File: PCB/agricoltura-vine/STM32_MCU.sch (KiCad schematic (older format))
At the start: 33 parts, among them SW1 B3U-1000P, T1 BU2032SM-JJ-GTR, T2 20021121-00010C4LF, T3 0675031020, U1 STM32F446RET6, X1 ABM3B-8.000MHZ-B2-T, X2 ABS07-32.768KHZ-9-T

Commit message: Route Started Connectors Changed
Changed to QWIIC style connectors and adjusted pinning of RJ45s, but switching to screw terminal header in next commit. THis is a backup
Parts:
- removed SW1: B3U-1000P, AVR-KiCAD-Lib-Mech-Switches:B3U-1000P, symbol AVR-KiCAD-Lib-Mech-Switches:B3U-1000P
- added SW1: TL3301NF260QG, AVR-KiCAD-Lib-Mech-Switches:TL3301NF260QG, symbol AVR-KiCAD-Lib-Mech-Switches:TL3301NF260QG
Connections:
- net labels added: D+, D-, ID, NRST, OSC32_IN, OSC32_OUT, OSC_IN, OSC_OUT, VBUS, VCAP1
- wire segments 117 -> 124
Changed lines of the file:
@@
-	1    0    0    -1
-$EndComp
-$Comp
-L AVR-KiCAD-Lib-Mech-Switches:B3U-1000P SW1
-U 1 1 5EEC10BD
-P 5600 5400
-F 0 "SW1" H 5600 5550 50  0000 C CNN
-F 1 "B3U-1000P" H 5650 5350 50  0000 C CNN
-F 2 "AVR-KiCAD-Lib-Mech-Switches:B3U-1000P" H 5600 5400 50  0001 C CNN
-F 3 "https://omronfs.omron.com/en_US/ecb/products/pdf/en-b3u.pdf" H 5600 5400 50  0001 C CNN
-F 4 "0.98000" H 5700 5650 50  0001 C CNN "Cost QTY: 1"
-F 5 "0.59822" H 5800 5750 50  0001 C CNN "Cost QTY: 1000"
-F 6 "*" H 5900 5850 50  0001 C CNN "Cost QTY: 2500"
-F 7 "*" H 6000 5950 50  0001 C CNN "Cost QTY: 5000"
-F 8 "*" H 6100 6050 50  0001 C CNN "Cost QTY: 10000"
-F 9 "Omron Electronics Inc-EMC Div" H 6200 6150 50  0001 C CNN "MFR"
-F 10 "B3U-1000P" H 6300 6250 50  0001 C CNN "MFR#"
-F 11 "Digikey" H 6400 6350 50  0001 C CNN "Vendor"
-F 12 "SW1020CT-ND" H 6500 6450 50  0001 C CNN "Vendor #"
-F 13 "AVR" H 6600 6550 50  0001 C CNN "Designer"
-F 14 "1.6mm" H 6700 6650 50  0001 C CNN "Height"
-F 15 "6/15/2020" H 7800 7750 50  0001 C CNN "Date Created"
-F 16 "6/15/2020" H 6800 6750 50  0001 C CNN "Date Modified"
-F 17 "Yes" H 6900 6850 50  0001 C CNN "Lead-Free ?"
-F 18 "1" H 7000 6950 50  0001 C CNN "RoHS Levels"
-F 19 "SMT" H 7100 7050 50  0001 C CNN "Mounting"
-F 20 "2" H 7200 7150 50  0001 C CNN "Pin Count #"
-F 21 "Active" H 7300 7250 50  0001 C CNN "Status"
-F 22 "*" H 7400 7350 50  0001 C CNN "Tolerance"
-F 23 "Switch" H 7500 7450 50  0001 C CNN "Type"
-F 24 "*" H 7600 7550 50  0001 C CNN "Voltage"
-F 25 "Proprietary" H 7700 7700 50  0001 C CNN "Package"
-F 26 "Tactile Switch SPST-NO Top Actuated Surface Mount" H 8000 8000 50  0001 C CNN "Description"
-F 27 "B3U-1000P" H 7900 7900 50  0001 C CNN "_Value_"
-F 28 "*" H 8000 8000 50  0001 C CNN "Management_ID"
-	1    5600 5400
 	1    0    0    -1
 $EndComp
@@
 L power:GND #PWR010
 U 1 1 5EF64659
-P 5900 5850
-F 0 "#PWR010" H 5900 5600 50  0001 C CNN
-F 1 "GND" H 5905 5677 50  0000 C CNN
-F 2 "" H 5900 5850 50  0001 C CNN
-F 3 "" H 5900 5850 50  0001 C CNN
-	1    5900 5850
-	1    0    0    -1
-$EndComp
-Wire Wire Line
-	5900 5400 5900 5850
-Wire Wire Line
-	5900 5850 5300 5850
-Connection ~ 5900 5850
+P 6250 5950
+F 0 "#PWR010" H 6250 5700 50  0001 C CNN
+F 1 "GND" H 6255 5777 50  0000 C CNN
+F 2 "" H 6250 5950 50  0001 C CNN
+F 3 "" H 6250 5950 50  0001 C CNN
+	1    6250 5950
+	1    0    0    -1
+$EndComp
+Wire Wire Line
+	6250 5500 6250 5950
+Wire Wire Line
+	6250 5950 5650 5950
+Connection ~ 6250 5950
 $Comp
 L AVR-KiCAD-Lib-Capacitors:C0402C104K9PACTU C13
@@
 	1    0    0    -1
 $EndComp
+Text Label 8800 2950 0    50   ~ 0
+D-
+Text Label 8800 3050 0    50   ~ 0
+D+
+Text Label 8800 3150 0    50   ~ 0
+ID
+Text Label 8800 2850 0    50   ~ 0
+VBUS
+Text Label 4650 5400 0    50   ~ 0
+NRST
+Text Label 1650 5400 0    50   ~ 0
+OSC_IN
+Text Label 1650 5550 0    50   ~ 0
+OSC_OUT
+Text Label 6850 3850 0    50   ~ 0
+OSC32_IN
+Text Label 6650 4500 1    50   ~ 0
+OSC32_OUT
+Text Label 7550 4100 1    50   ~ 0
+VCAP1
+$Comp
+L AVR-KiCAD-Lib-Mech-Switches:TL3301NF260QG SW1
+U 1 1 5EF8B26F
+P 5950 5400
+F 0 "SW1" H 5950 5550 50  0000 C CNN
+F 1 "TL3301NF260QG" H 6600 5250 50  0000 C CNN
+F 2 "AVR-KiCAD-Lib-Mech-Switches:TL3301NF260QG" H 5950 5400 50  0001 C CNN
+F 3 "http://spec_sheets.e-switch.com/specs/P010517.pdf" H 5950 5400 50  0001 C CNN
+F 4 "0.38000" H 6050 5650 50  0001 C CNN "Cost QTY: 1"
+F 5 "*" H 6150 5750 50  0001 C CNN "Cost QTY: 1000"
+F 6 "*" H 6250 5850 50  0001 C CNN "Cost QTY: 2500"
+F 7 "*" H 6350 5950 50  0001 C CNN "Cost QTY: 5000"
+F 8 "*" H 6450 6050 50  0001 C CNN "Cost QTY: 10000"
+F 9 "E-Switch" H 6550 6150 50  0001 C CNN "MFR"
+F 10 "TL3301NF260QG" H 6650 6250 50  0001 C CNN "MFR#"
+F 11 "Digikey" H 6750 6350 50  0001 C CNN "Vendor"
+F 12 "EG1868TR-ND" H 6850 6450 50  0001 C CNN "Vendor #"
+F 13 "AVR" H 6950 6550 50  0001 C CNN "Designer"
+F 14 "4.4mm" H 7050 6650 50  0001 C CNN "Height"
+F 15 "2/28/2020" H 8150 7750 50  0001 C CNN "Date Created"
+F 16 "2/28/2020" H 7150 6750 50  0001 C CNN "Date Modified"
+F 17 "Yes" H 7250 6850 50  0001 C CNN "Lead-Free ?"
+F 18 "1" H 7350 6950 50  0001 C CNN "RoHS Levels"
+F 19 "SMT" H 7450 7050 50  0001 C CNN "Mounting"
+F 20 "4" H 7550 7150 50  0001 C CNN "Pin Count #"
+F 21 "Active" H 7650 7250 50  0001 C CNN "Status"
+F 22 "*" H 7750 7350 50  0001 C CNN "Tolerance"
+F 23 "Mechanical Momentary Switch " H 7850 7450 50  0001 C CNN "Type"
+F 24 "12VDC" H 7950 7550 50  0001 C CNN "Voltage"
+F 25 "Proprietary" H 8050 7700 50  0001 C CNN "Package"
+F 26 "Tactile Switch SPST-NO Top Actuated Surface Mount" H 8350 8000 50  0001 C CNN "Description"
+F 27 "TL3301NF260QG" H 8250 7900 50  0001 C CNN "_Value_"
+F 28 "*" H 8350 8000 50  0001 C CNN "Management_ID"
+	1    5950 5400
+	1    0    0    -1
+$EndComp
+Wire Wire Line
+	5650 5950 5650 5500
+Wire Wire Line
+	5300 5400 5650 5400
+Wire Wire Line
+	5650 5400 5650 5150
+Wire Wire Line
+	5650 5150 6250 5150
+Wire Wire Line
+	6250 5150 6250 5400
+Connection ~ 5650 5400
+Wire Wire Line
+	5300 5850 5300 5950
+Wire Wire Line
+	5300 5950 5650 5950
+Connection ~ 5650 5950
 $EndSCHEMATC

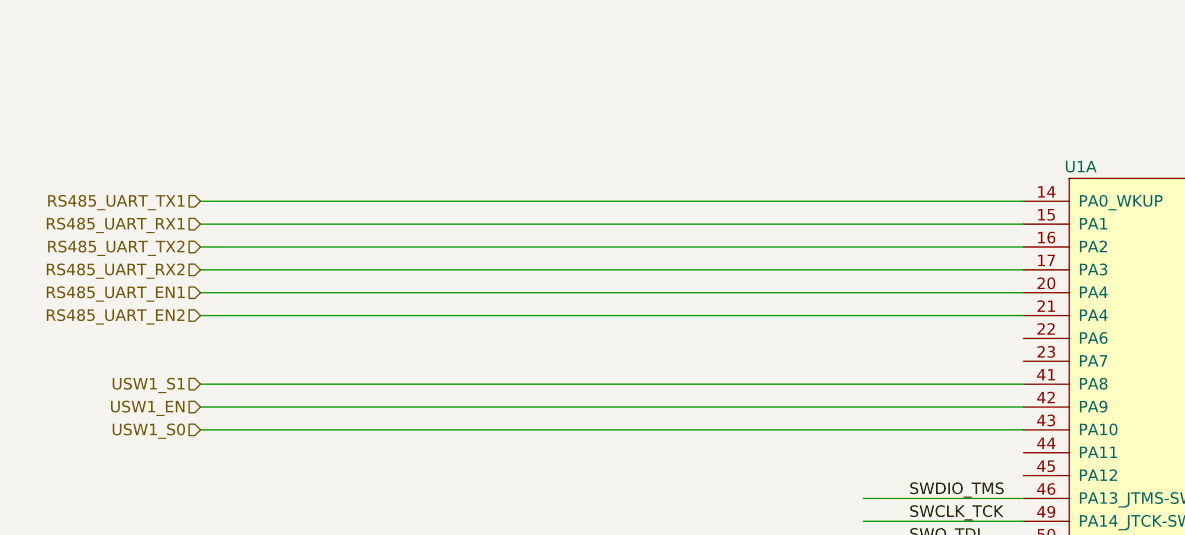
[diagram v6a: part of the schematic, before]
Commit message: Routing and New RS485
swapped over the RS485 chip to a new one and started routing the board.
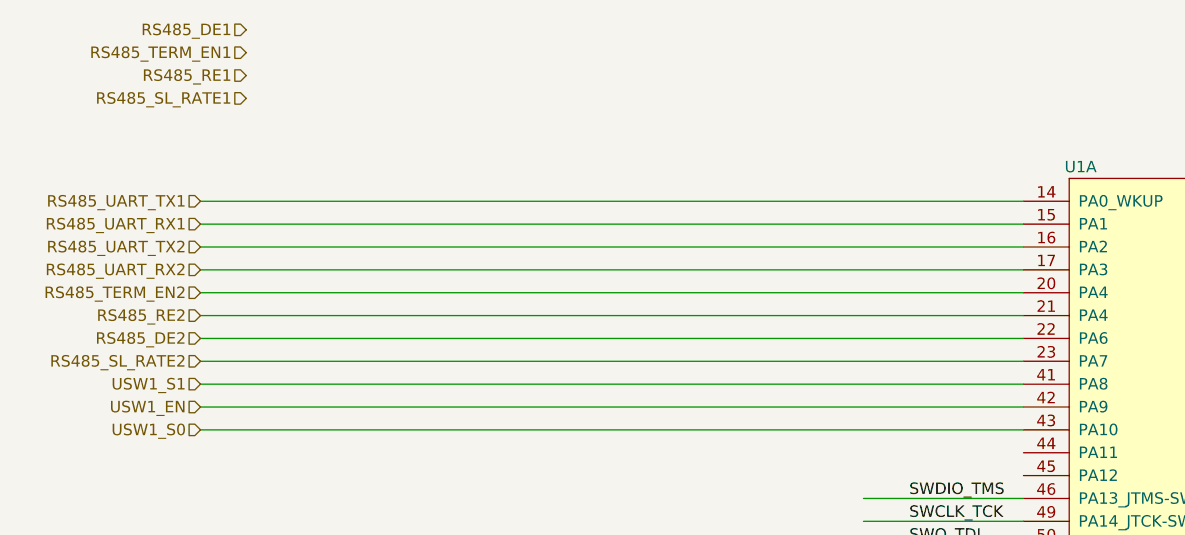
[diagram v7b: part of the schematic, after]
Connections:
- net labels added: RS485_DE1, RS485_DE2, RS485_RE1, RS485_RE2, RS485_SL_RATE1, RS485_SL_RATE2, RS485_TERM_EN1, RS485_TERM_EN2
- net labels removed: RS485_UART_EN1, RS485_UART_EN2
- wire segments 124 -> 126
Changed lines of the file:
@@
 Text HLabel 1200 3850 0    50   Input ~ 0
 UART_SENSE1_TX
-Text HLabel 1200 1950 0    50   Input ~ 0
-RS485_UART_EN1
 Text HLabel 1200 1550 0    50   Input ~ 0
 RS485_UART_TX1
 Text HLabel 1200 1650 0    50   Input ~ 0
 RS485_UART_RX1
-Text HLabel 1200 2050 0    50   Input ~ 0
-RS485_UART_EN2
 Text HLabel 1200 1750 0    50   Input ~ 0
 RS485_UART_TX2
@@
 	4800 1850 1200 1850
 Wire Wire Line
-	1200 1950 4800 1950
-Wire Wire Line
-	4800 2050 1200 2050
-Wire Wire Line
 	4800 3950 1200 3950
 Wire Wire Line
@@
 	5300 5950 5650 5950
 Connection ~ 5650 5950
+Text HLabel 1400 800  0    50   Input ~ 0
+RS485_DE1
+Text HLabel 1200 2150 0    50   Input ~ 0
+RS485_DE2
+Text HLabel 1400 900  0    50   Input ~ 0
+RS485_TERM_EN1
+Text HLabel 1400 1100 0    50   Input ~ 0
+RS485_SL_RATE1
+Text HLabel 1400 1000 0    50   Input ~ 0
+RS485_RE1
+Text HLabel 1200 2250 0    50   Input ~ 0
+RS485_SL_RATE2
+Text HLabel 1200 2050 0    50   Input ~ 0
+RS485_RE2
+Text HLabel 1200 1950 0    50   Input ~ 0
+RS485_TERM_EN2
+Wire Wire Line
+	4800 1950 1200 1950
+Wire Wire Line
+	1200 2050 4800 2050
+Wire Wire Line
+	1200 2150 4800 2150
+Wire Wire Line
+	4800 2250 1200 2250
 $EndSCHEMATC

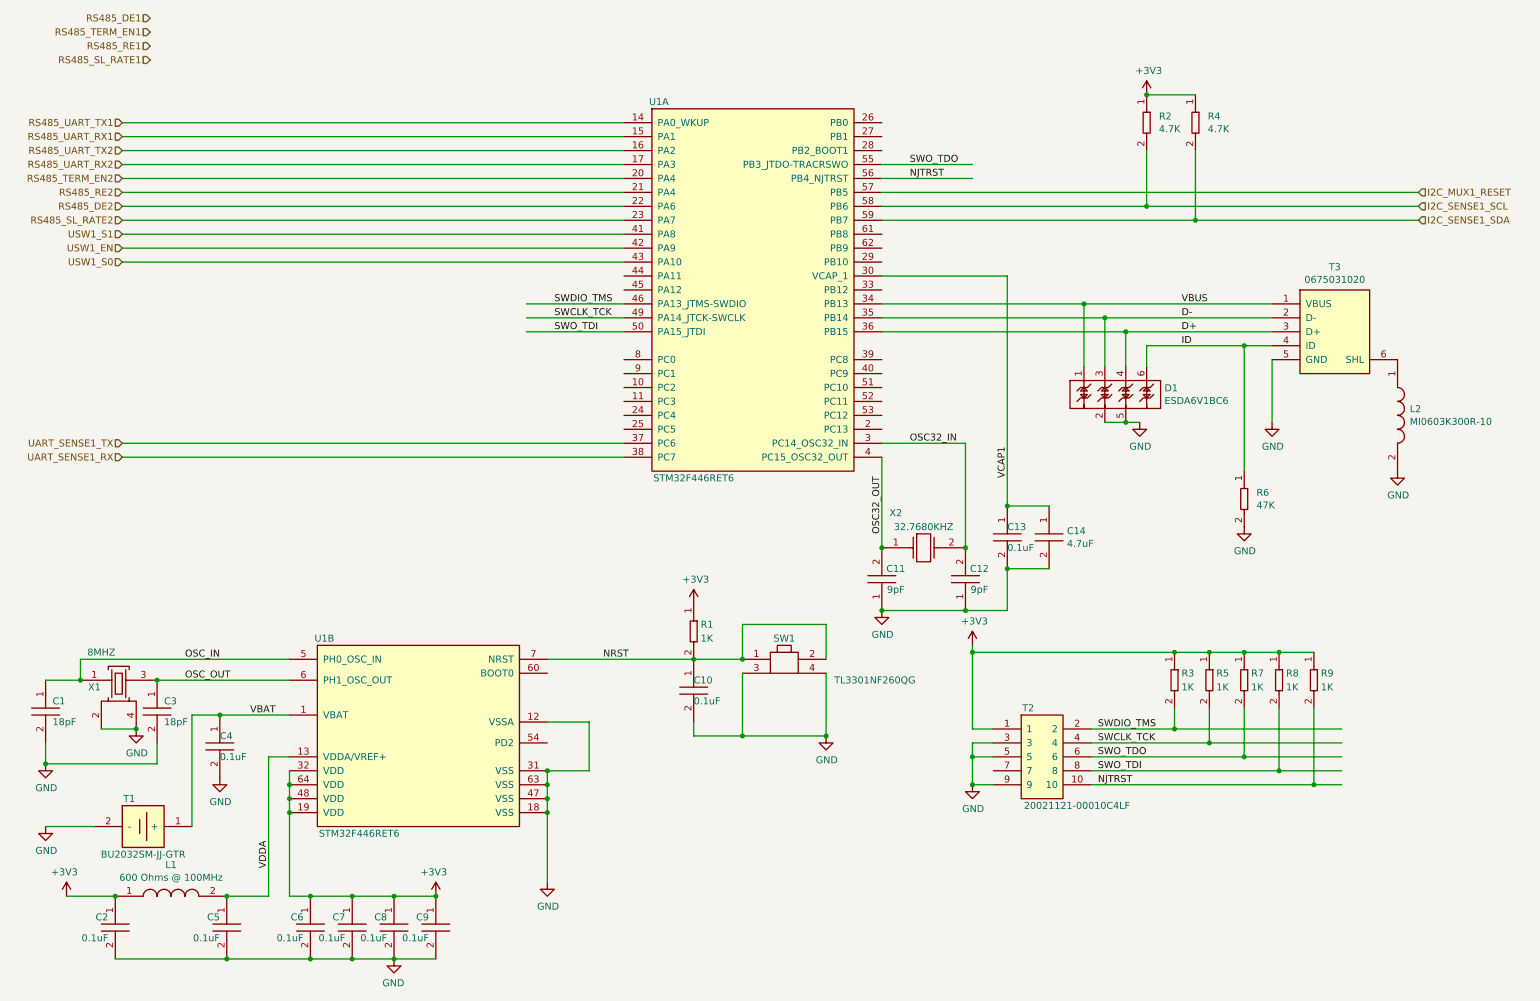
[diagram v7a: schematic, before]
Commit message: Routing progress
RS845 ports routed, UART mux routed, sensor ports reoriented. Starting to come together.
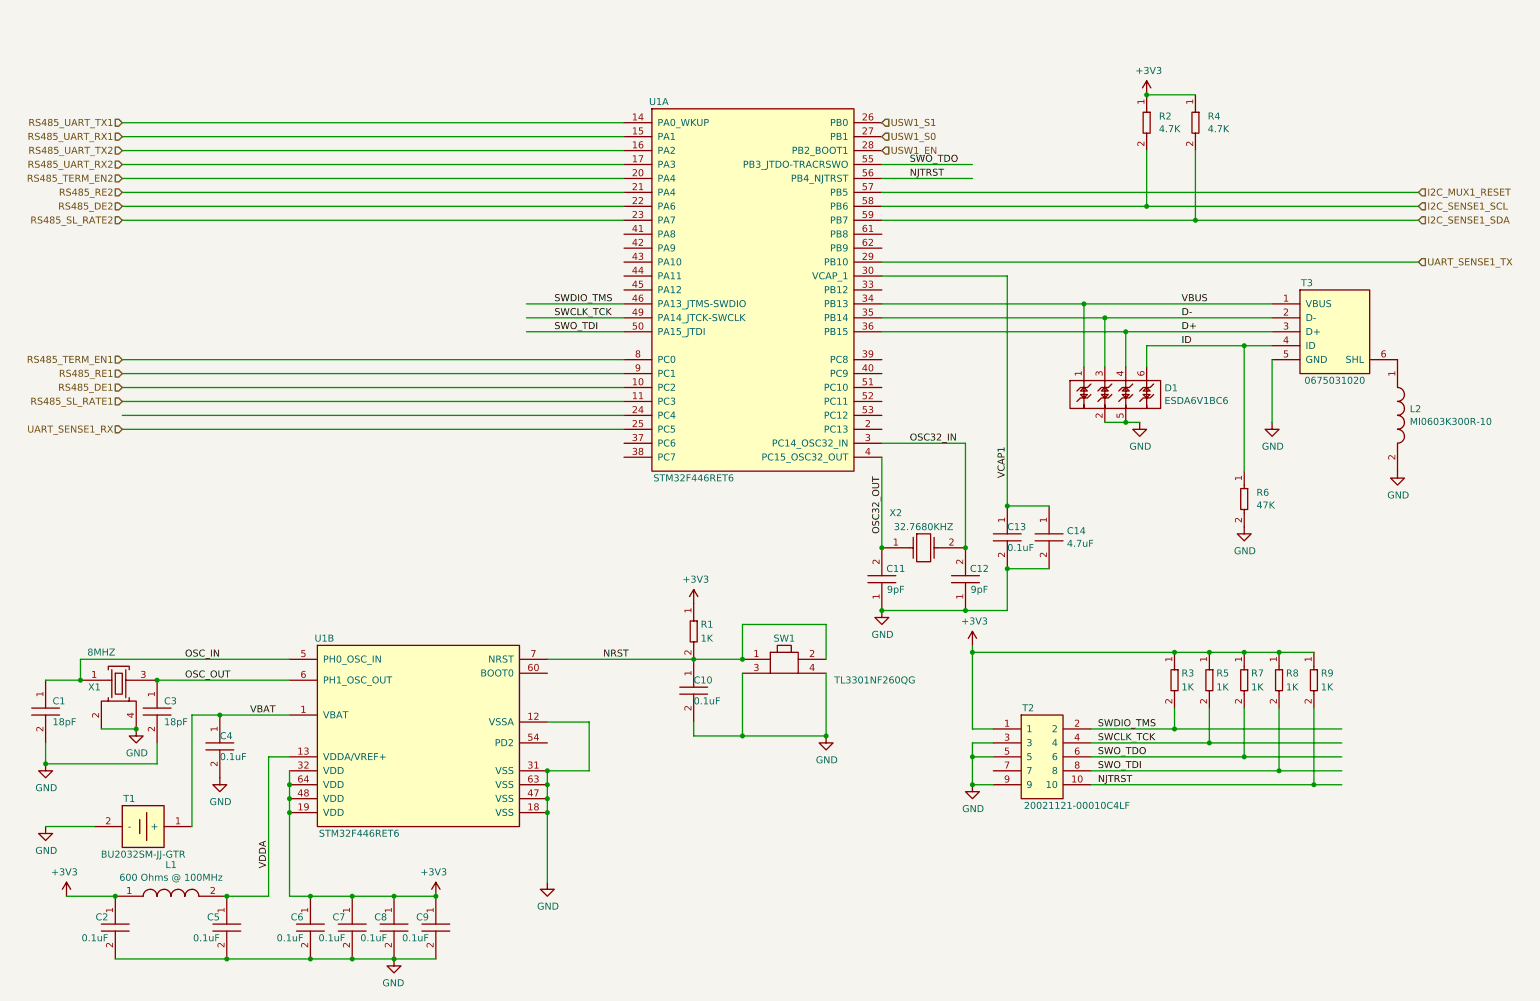
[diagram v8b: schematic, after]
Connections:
- wire segments 126 -> 128
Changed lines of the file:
@@
 U 1 1 5EF8842D
 P 9650 2750
-F 0 "T3" H 9900 2915 50  0000 C CNN
-F 1 "0675031020" H 9900 2824 50  0000 C CNN
+F 0 "T3" H 9700 2800 50  0000 C CNN
+F 1 "0675031020" H 9900 2100 50  0000 C CNN
 F 2 "AVR-KiCAD-Lib-Connectors:USB_Mini-B" H 9450 2750 50  0001 C CNN
 F 3 "https://www.molex.com/pdm_docs/sd/675031020_sd.pdf" H 9550 2850 50  0001 C CNN
@@
 	8400 3700 8250 3700
 Connection ~ 7550 4300
-Text HLabel 1200 3850 0    50   Input ~ 0
+Text HLabel 10500 2550 2    50   Input ~ 0
 UART_SENSE1_TX
 Text HLabel 1200 1550 0    50   Input ~ 0
@@
 Wire Wire Line
 	4800 1850 1200 1850
-Wire Wire Line
-	4800 3950 1200 3950
-Wire Wire Line
-	4800 3850 1200 3850
-Text HLabel 1200 2450 0    50   Input ~ 0
+Text HLabel 6650 1750 2    50   Input ~ 0
 USW1_EN
-Text HLabel 1200 2550 0    50   Input ~ 0
+Text HLabel 6650 1650 2    50   Input ~ 0
 USW1_S0
-Text HLabel 1200 2350 0    50   Input ~ 0
+Text HLabel 6650 1550 2    50   Input ~ 0
 USW1_S1
-Text HLabel 1200 3950 0    50   Input ~ 0
+Text HLabel 1200 3750 0    50   Input ~ 0
 UART_SENSE1_RX
 Wire Wire Line
-	1200 2350 4800 2350
-Wire Wire Line
-	1200 2450 4800 2450
-Wire Wire Line
-	1200 2550 4800 2550
+	1200 3650 4800 3650
 $Comp
 L AVR-KiCAD-Lib-Capacitors:C0402C104K9PACTU C5
@@
 	5300 5950 5650 5950
 Connection ~ 5650 5950
-Text HLabel 1400 800  0    50   Input ~ 0
+Text HLabel 1200 3450 0    50   Input ~ 0
 RS485_DE1
 Text HLabel 1200 2150 0    50   Input ~ 0
 RS485_DE2
-Text HLabel 1400 900  0    50   Input ~ 0
+Text HLabel 1200 3250 0    50   Input ~ 0
 RS485_TERM_EN1
-Text HLabel 1400 1100 0    50   Input ~ 0
+Text HLabel 1200 3550 0    50   Input ~ 0
 RS485_SL_RATE1
-Text HLabel 1400 1000 0    50   Input ~ 0
+Text HLabel 1200 3350 0    50   Input ~ 0
 RS485_RE1
 Text HLabel 1200 2250 0    50   Input ~ 0
@@
 Wire Wire Line
 	4800 2250 1200 2250
+Wire Wire Line
+	1200 3350 4800 3350
+Wire Wire Line
+	1200 3450 4800 3450
+Wire Wire Line
+	1200 3550 4800 3550
+Wire Wire Line
+	4800 3250 1200 3250
+Wire Wire Line
+	4800 3750 1200 3750
+Wire Wire Line
+	6650 2550 10500 2550
 $EndSCHEMATC
